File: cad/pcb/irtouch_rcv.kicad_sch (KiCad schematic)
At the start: 69 parts, among them Q1 Q_Photo_NPN, Q10 Q_Photo_NPN, Q11 Q_Photo_NPN, Q12 Q_Photo_NPN, Q13 Q_Photo_NPN, Q14 Q_Photo_NPN, Q15 Q_Photo_NPN, Q16 Q_Photo_NPN, Q17 Q_Photo_NPN, Q18 Q_Photo_NPN, Q19 Q_Photo_NPN, Q2 Q_Photo_NPN, Q20 Q_Photo_NPN, Q21 Q_Photo_NPN, Q22 Q_Photo_NPN, Q23 Q_Photo_NPN, Q24 Q_Photo_NPN, Q25 Q_Photo_NPN, Q26 Q_Photo_NPN, Q27 Q_Photo_NPN, Q28 Q_Photo_NPN, Q29 Q_Photo_NPN, Q3 Q_Photo_NPN, Q30 Q_Photo_NPN, Q31 Q_Photo_NPN, Q32 Q_Photo_NPN, Q4 Q_Photo_NPN, Q5 Q_Photo_NPN, Q6 Q_Photo_NPN, Q7 Q_Photo_NPN, Q8 Q_Photo_NPN, Q9 Q_Photo_NPN, U1 74HC4051PW,118, U2 74HC4051PW,118, U3 74HC4051PW,118, U4 74HC4051PW,118

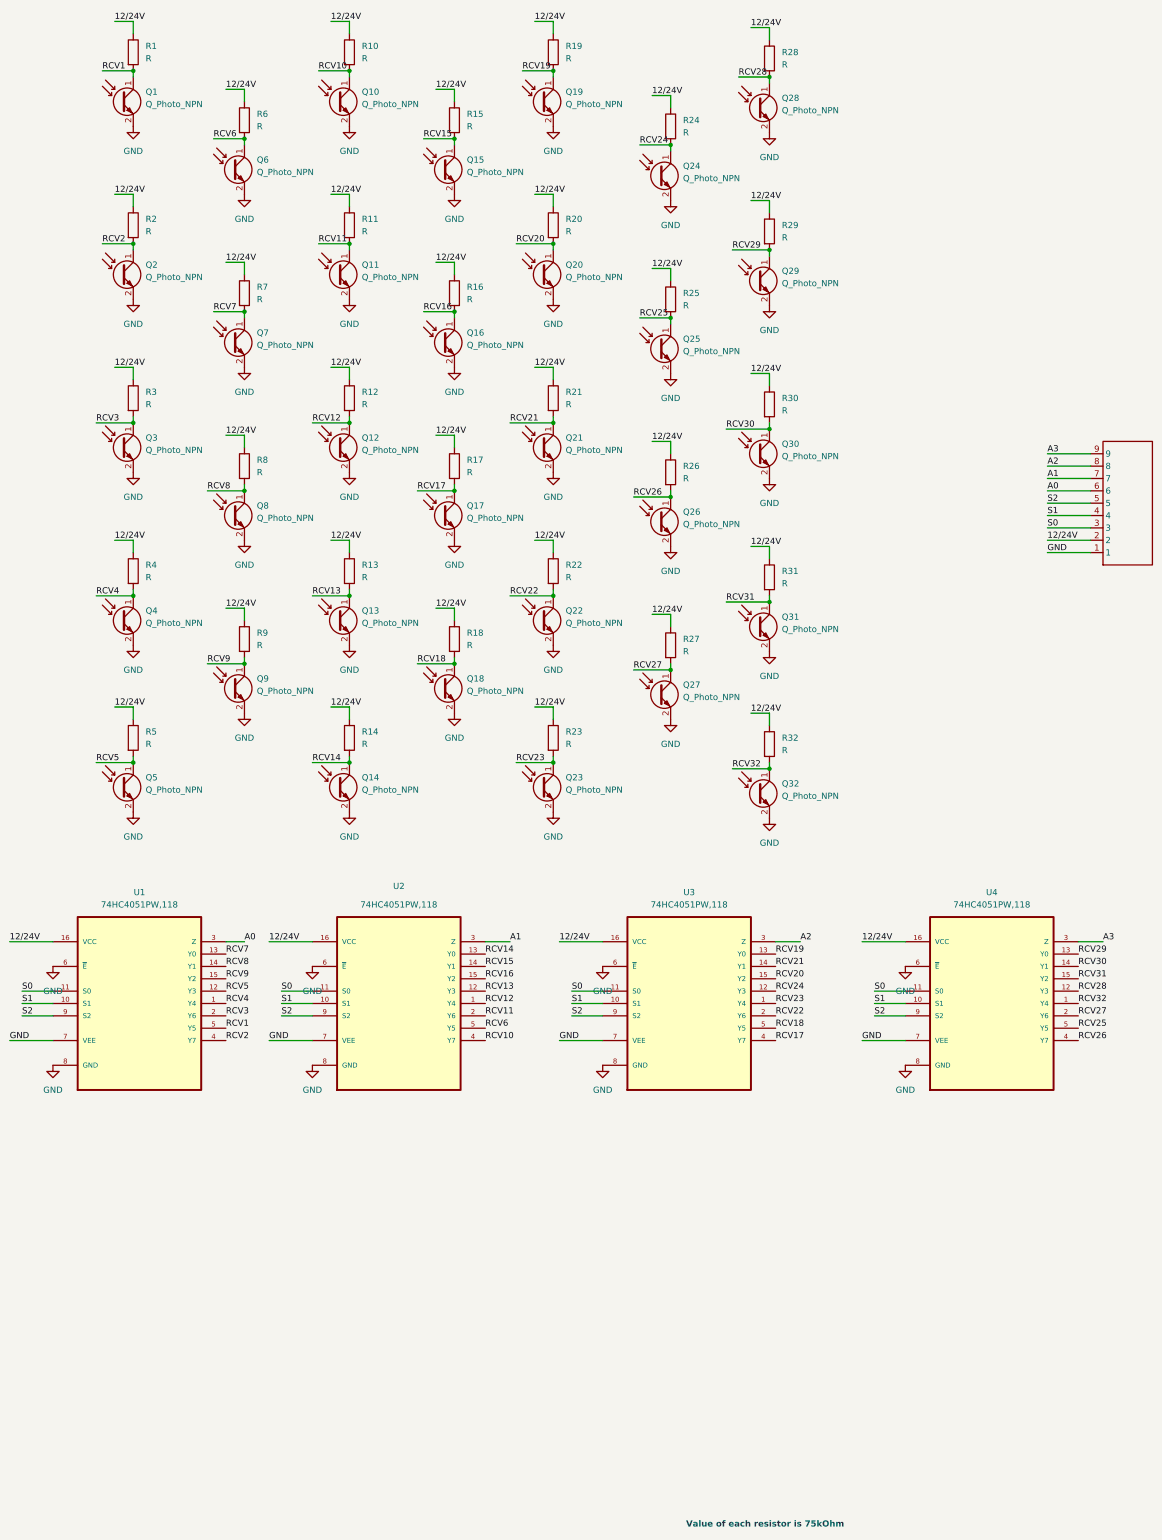
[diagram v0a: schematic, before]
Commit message: added Arduino breakout pcb, updated irtouch_rcv design to 2-layer
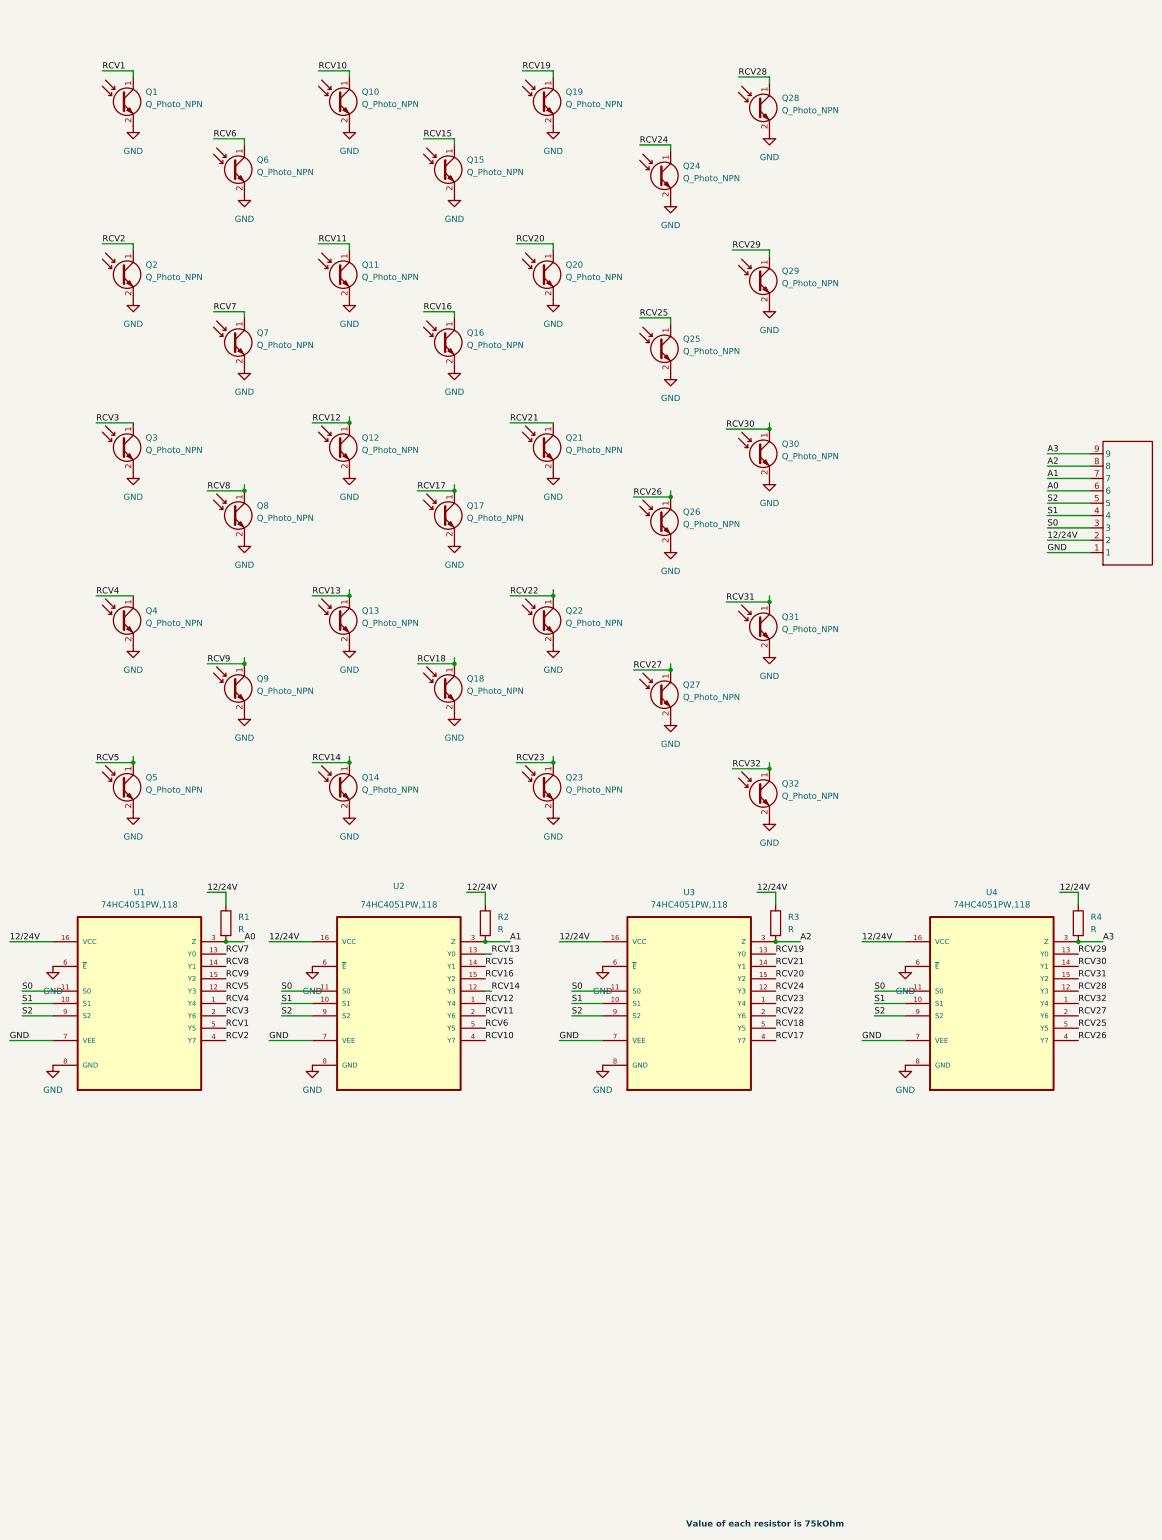
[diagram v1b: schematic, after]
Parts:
- removed R10, R11, R12, R13, R14, R15, R16, R17, R18, R19, R20, R21, R22, R23, R24, R25, R26, R27, R28, R29, R30, R31, R32, R5, R6, R7, R8, R9: R, IRTouch:R0603, symbol Device:R
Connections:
- net A0: now also R1.2
- net A1: now also R2.2
- net A2: now also R3.2
- net A3: now also R4.2
- net RCV1: no longer R1.2
- net RCV13: now also U2.13 (Y0); no longer U2.12 (Y3)
- net RCV14: now also U2.12 (Y3); no longer U2.13 (Y0)
- net RCV2: no longer R2.2
- net RCV3: no longer R3.2
- net RCV4: no longer R4.2
